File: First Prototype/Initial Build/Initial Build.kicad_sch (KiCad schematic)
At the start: 33 parts, among them J2 Conn_02x04_Odd_Even, Q1 MPSA44, Q2 BC328, Q3 BC517, U1 TLC555xP, U2 TLC555xP

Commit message: added pic
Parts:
- added C8: 47n, Capacitor_THT:C_Disc_D6.0mm_W2.5mm_P5.00mm, symbol Device:C
- added J1: Conn_01x06, symbol Connector_Generic:Conn_01x06
- added R13, R14, R15: 330k, Capacitor_SMD:C_0805_2012Metric, symbol Device:R
- added R16: 3k9, Capacitor_SMD:C_0805_2012Metric, symbol Device:R
- added R17, R18: 10k, Capacitor_SMD:C_0805_2012Metric, symbol Device:R
- added U3: PIC12F1822-ISN, Package_DIP:DIP-8_W7.62mm, symbol MCU_Microchip_PIC12:PIC12F1822-ISN
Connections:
- net +3.3VA: now also C8.1, J1.2 (Pin_2), U3.1 (VDD)
- net 400V: now also R13.1
- net GND: now also C8.2, J1.3 (Pin_3), R16.2, U3.8 (VSS)
- net Pulse A: now also U3.5 (RA2)
- net Pulse B: now also J1.1 (Pin_1), U3.4 (RA3)
- net PWM: now reaches Q1.2 (B), R2.1, U1.7 (DIS)
- net PWM: now also U3.2 (RA5)
- new net: R15.2, R16.1, U3.3 (RA4)
- new net: R13.2, R14.1
- new net: R14.2, R15.1
- new net: J1.4 (Pin_4), R17.2, U3.7 (RA0)
- new net: J1.5 (Pin_5), R18.2, U3.6 (RA1)
- new net USART_RX: R18.1
- new net USART_TX: R17.1
- no-connect marks 5 -> 6

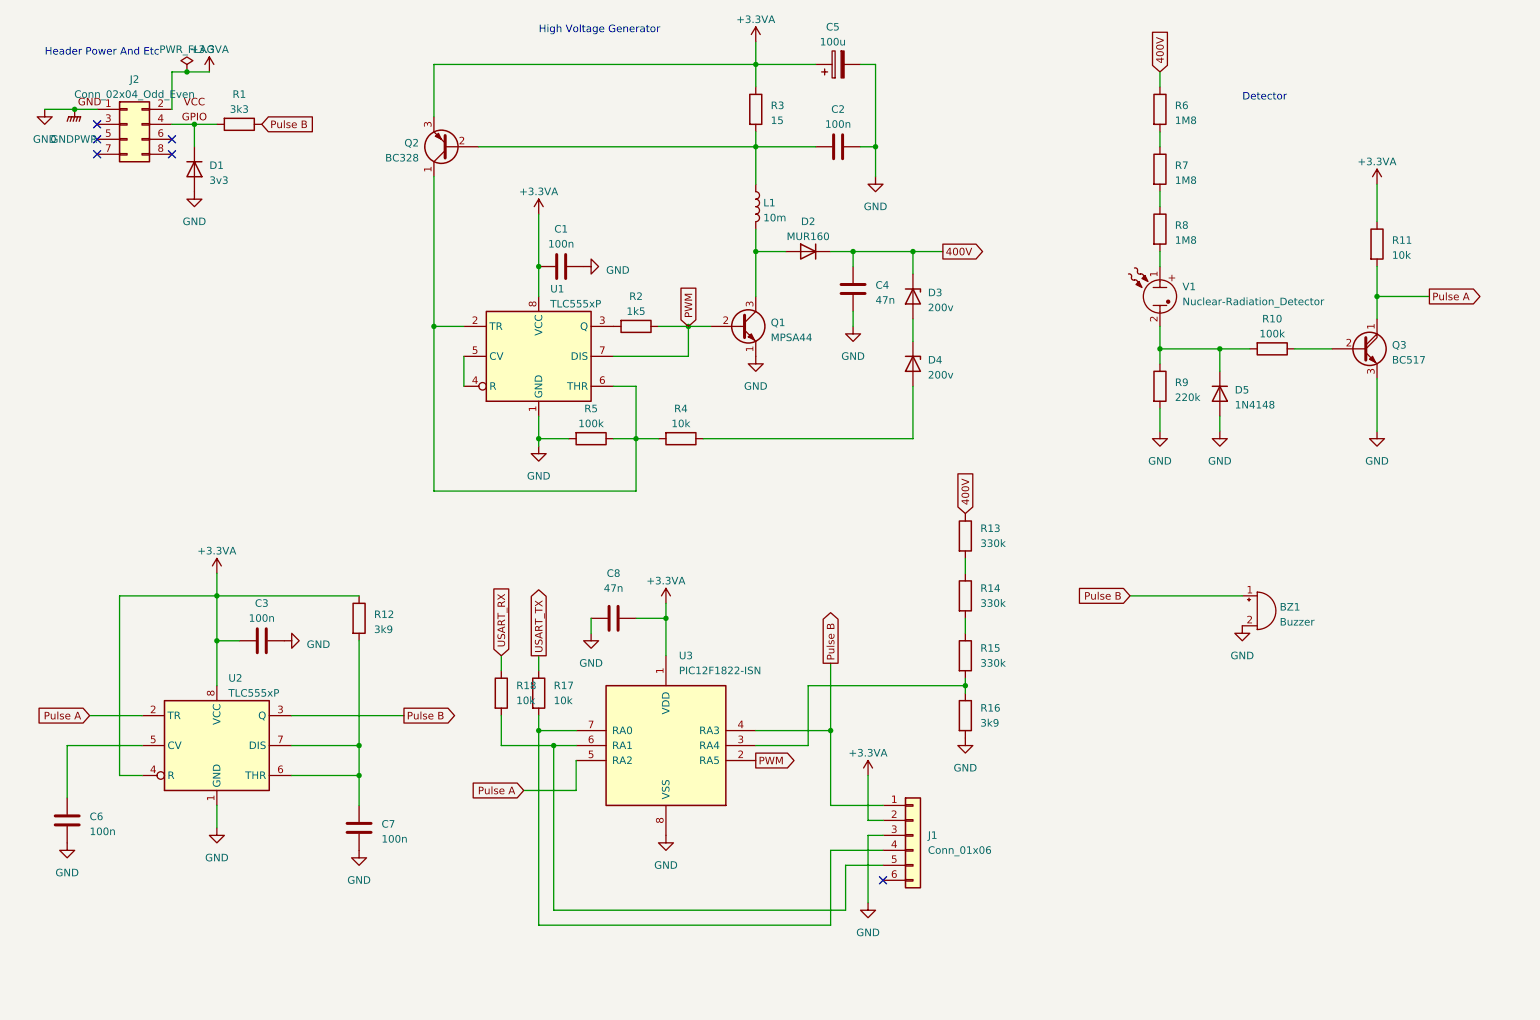
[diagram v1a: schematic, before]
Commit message: removed non-pic related components added indicator for 400v
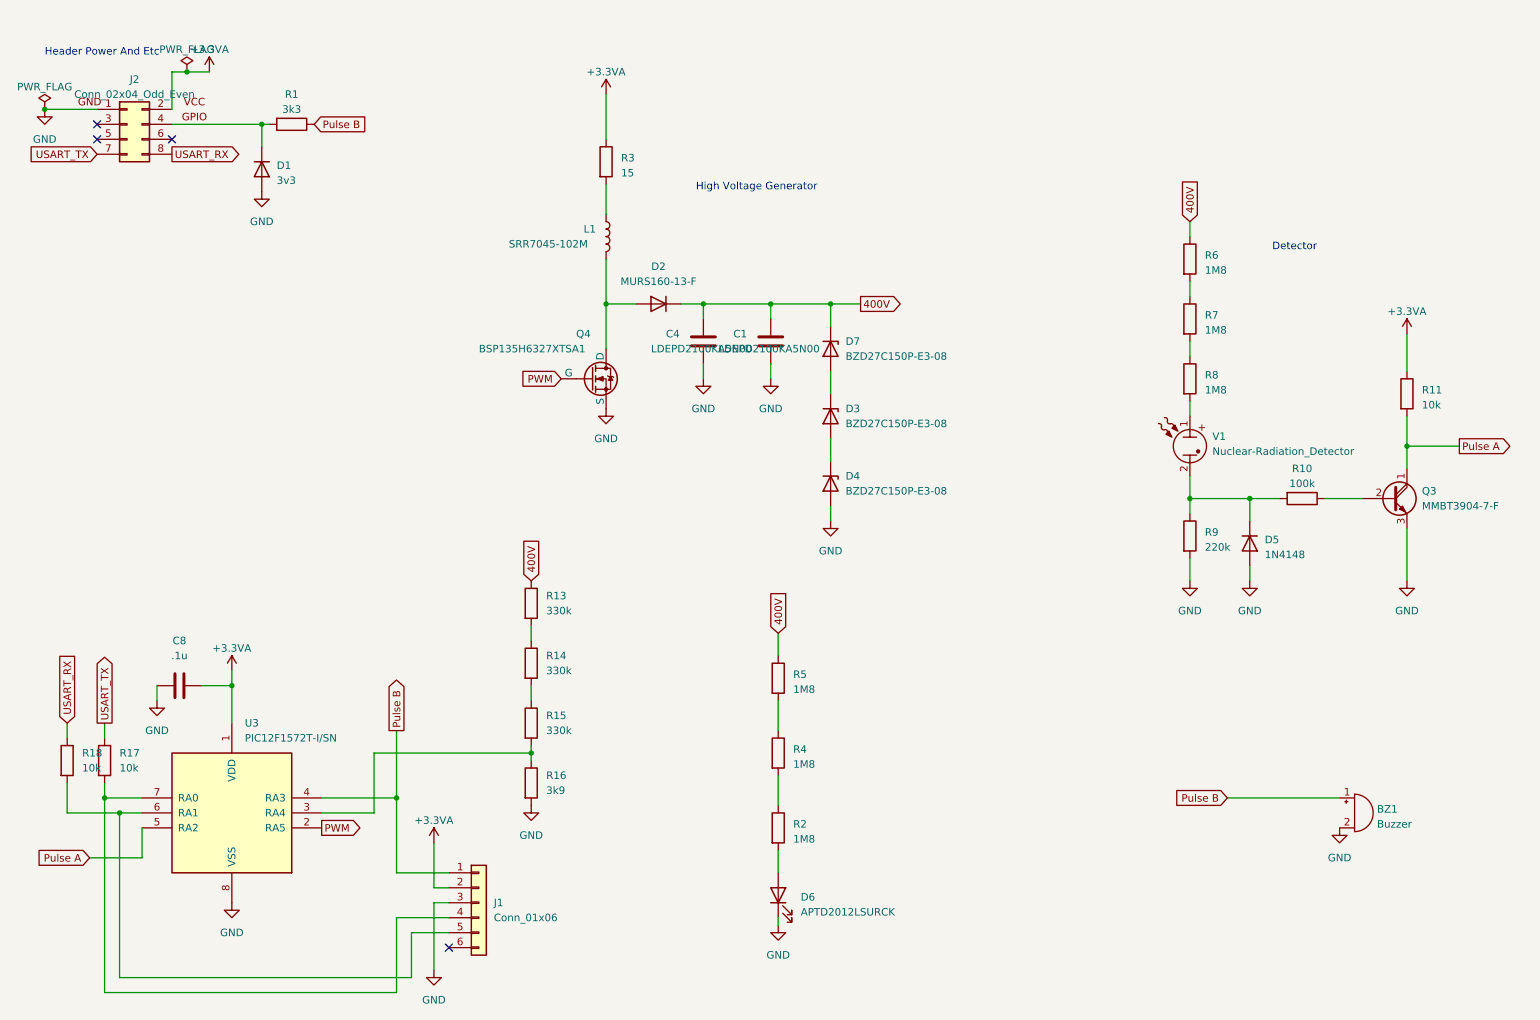
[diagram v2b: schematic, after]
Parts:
- removed C2: 100n, Capacitor_THT:C_Disc_D6.0mm_W4.4mm_P5.00mm, symbol Device:C
- removed C3, C6, C7: 100n, Capacitor_SMD:C_0805_2012Metric, symbol Device:C
- removed C5: 100u, Capacitor_THT:C_Disc_D6.0mm_W2.5mm_P5.00mm, symbol Device:C_Polarized
- removed D3, D4: 200v, Diode_SMD:D_SMF, symbol Device:D_Zener
- removed Q1: MPSA44, Package_TO_SOT_THT:TO-92_Inline, symbol Transistor_BJT:MPSA42
- removed Q2: BC328, Package_TO_SOT_THT:TO-92_Inline, symbol Transistor_BJT:BC328
- removed R12: 3k9, Capacitor_SMD:C_0805_2012Metric, symbol Device:R
- removed U1, U2: TLC555xP, Package_DIP:DIP-8_W7.62mm, symbol Timer:TLC555xP
- added D3, D4, D7: BZD27C150P-E3-08, Diode_SMD:D_SMF, symbol Diode:BZD27Cxx
- added D6: APTD2012LSURCK, LED_SMD:LED_0805_2012Metric_Pad1.15x1.40mm_HandSolder, symbol Device:LED
- added Q4: BSP135H6327XTSA1, Package_TO_SOT_SMD:SOT-223, symbol Simulation_SPICE:NMOS
- C1: value 100n -> LDEPD2100KA5N00; footprint Capacitor_SMD:C_0805_2012Metric -> Capacitor_SMD:C_2220_5650Metric_Pad1.97x5.40mm_HandSolder
- C4: value 47n -> LDEPD2100KA5N00; footprint Capacitor_THT:C_Disc_D6.0mm_W2.5mm_P5.00mm -> Capacitor_SMD:C_2220_5650Metric_Pad1.97x5.40mm_HandSolder
- C8: value 47n -> .1u; footprint Capacitor_THT:C_Disc_D6.0mm_W2.5mm_P5.00mm -> Capacitor_SMD:C_0805_2012Metric_Pad1.18x1.45mm_HandSolder
- D1: footprint Diode_SMD:D_SOD-123F -> Diode_SMD:D_SMB-SMC_Universal_Handsoldering
- D2: value MUR160 -> MURS160-13-F; footprint Diode_THT:D_DO-41_SOD81_P10.16mm_Horizontal -> Diode_SMD:D_SMB_Handsoldering
- D5: footprint Diode_THT:D_DO-35_SOD27_P7.62mm_Horizontal -> Diode_SMD:D_SMB-SMC_Universal_Handsoldering
- J1: footprint (none) -> Connector_PinHeader_2.54mm:PinHeader_1x06_P2.54mm_Vertical
- L1: value 10m -> SRR7045-102M; footprint Inductor_THT:L_Axial_L12.0mm_D5.0mm_P5.08mm_Vertical_Fastron_MISC -> Inductor_SMD:L_7.3x7.3_H3.5
- Q3: value BC517 -> MMBT3904-7-F; footprint Package_TO_SOT_THT:TO-92_Inline -> Package_TO_SOT_SMD:SOT-23-3
- R1: footprint Resistor_SMD:R_0805_2012Metric -> Resistor_SMD:R_1206_3216Metric_Pad1.30x1.75mm_HandSolder
- R10, R11, R13, R14, R15, R16, R17, R18, R3, R6, R7, R8, R9: footprint Capacitor_SMD:C_0805_2012Metric -> Resistor_SMD:R_1206_3216Metric_Pad1.30x1.75mm_HandSolder
- R2: value 1k5 -> 1M8; footprint Capacitor_SMD:C_0805_2012Metric -> Resistor_SMD:R_1206_3216Metric_Pad1.30x1.75mm_HandSolder
- R4: value 10k -> 1M8; footprint Capacitor_SMD:C_0805_2012Metric -> Resistor_SMD:R_1206_3216Metric_Pad1.30x1.75mm_HandSolder
- R5: value 100k -> 1M8; footprint Capacitor_SMD:C_0805_2012Metric -> Resistor_SMD:R_1206_3216Metric_Pad1.30x1.75mm_HandSolder
- U3: value PIC12F1822-ISN -> PIC12F1572T-I/SN; footprint Package_DIP:DIP-8_W7.62mm -> Package_SO:SOIC-8_3.9x4.9mm_P1.27mm
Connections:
- net +3.3VA: no longer C1.2
- net 400V: now also C1.2, R5.1, D7.1 (K)
- net GND: now also D4.2 (A), D6.1 (K), Q4.3 (S); no longer R5.2
- net PWM: now also Q4.2 (G); no longer R2.1
- net USART_RX: now also J2.8 (FUTURE)
- net USART_TX: now also J2.7 (Future)
- net at D2.2 (A), L1.2: now also Q4.1 (D)
- net at R4.2: now also R2.1; no longer R5.1
- net at R2.2: now also D6.2 (A)
- net at R4.1: now also R5.2
- new net: D3.2 (A), D4.1 (K)
- new net: D3.1 (K), D7.2 (A)
- no-connect marks 6 -> 4
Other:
- moved on the sheet: BZ1, C4, C8, D1, D2, D5, J1, Q3, R1, R10, R11, R13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

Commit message: updated tube fp began routing
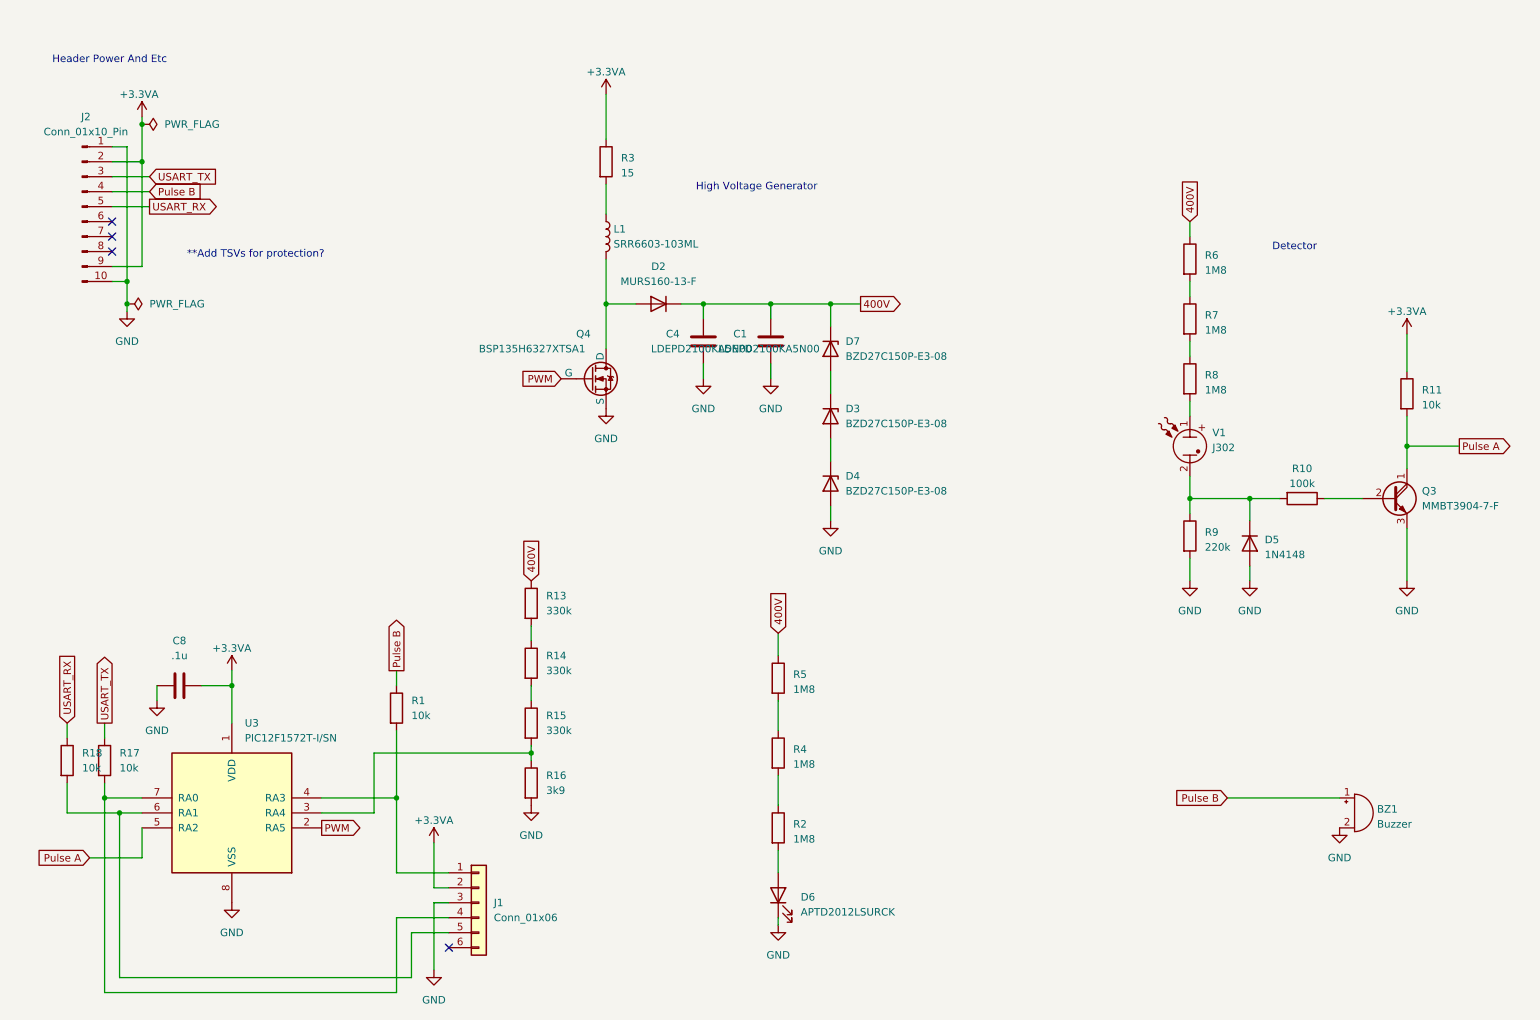
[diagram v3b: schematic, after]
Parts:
- removed D1: 3v3, Diode_SMD:D_SMB-SMC_Universal_Handsoldering, symbol Device:D
- removed J2: Conn_02x04_Odd_Even, Connector_IDC:IDC-Header_2x05_P2.54mm_Vertical, symbol Connector_Generic:Conn_02x04_Odd_Even
- added J2: Conn_01x10_Pin, Connector_PinHeader_2.54mm:PinHeader_2x05_P2.54mm_Vertical, symbol Connector:Conn_01x10_Pin
- L1: value SRR7045-102M -> SRR6603-103ML; footprint Inductor_SMD:L_7.3x7.3_H3.5 -> Inductor_SMD:L_Bourns_SRP7028A_7.3x6.6mm
- R1: value 3k3 -> 10k
- V1: value Nuclear-Radiation_Detector -> J302; footprint Geiger:Geiger Clips -> Geiger:Geiger_Clips
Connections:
- net +3.3VA: now also J2.2 (Pin_2), J2.9 (Pin_9)
- net GND: now also J2.1 (Pin_1), J2.10 (Pin_10)
- net Pulse B: now also J2.4 (Pin_4); no longer J1.1 (Pin_1), U3.4 (RA3)
- net USART_RX: now also J2.5 (Pin_5)
- net USART_TX: now also J2.3 (Pin_3)
- net at R1.2: now also J1.1 (Pin_1), U3.4 (RA3)
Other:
- note added: "**Add TSVs for protection?"

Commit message: rotated esp moved resistors away from sd card holder
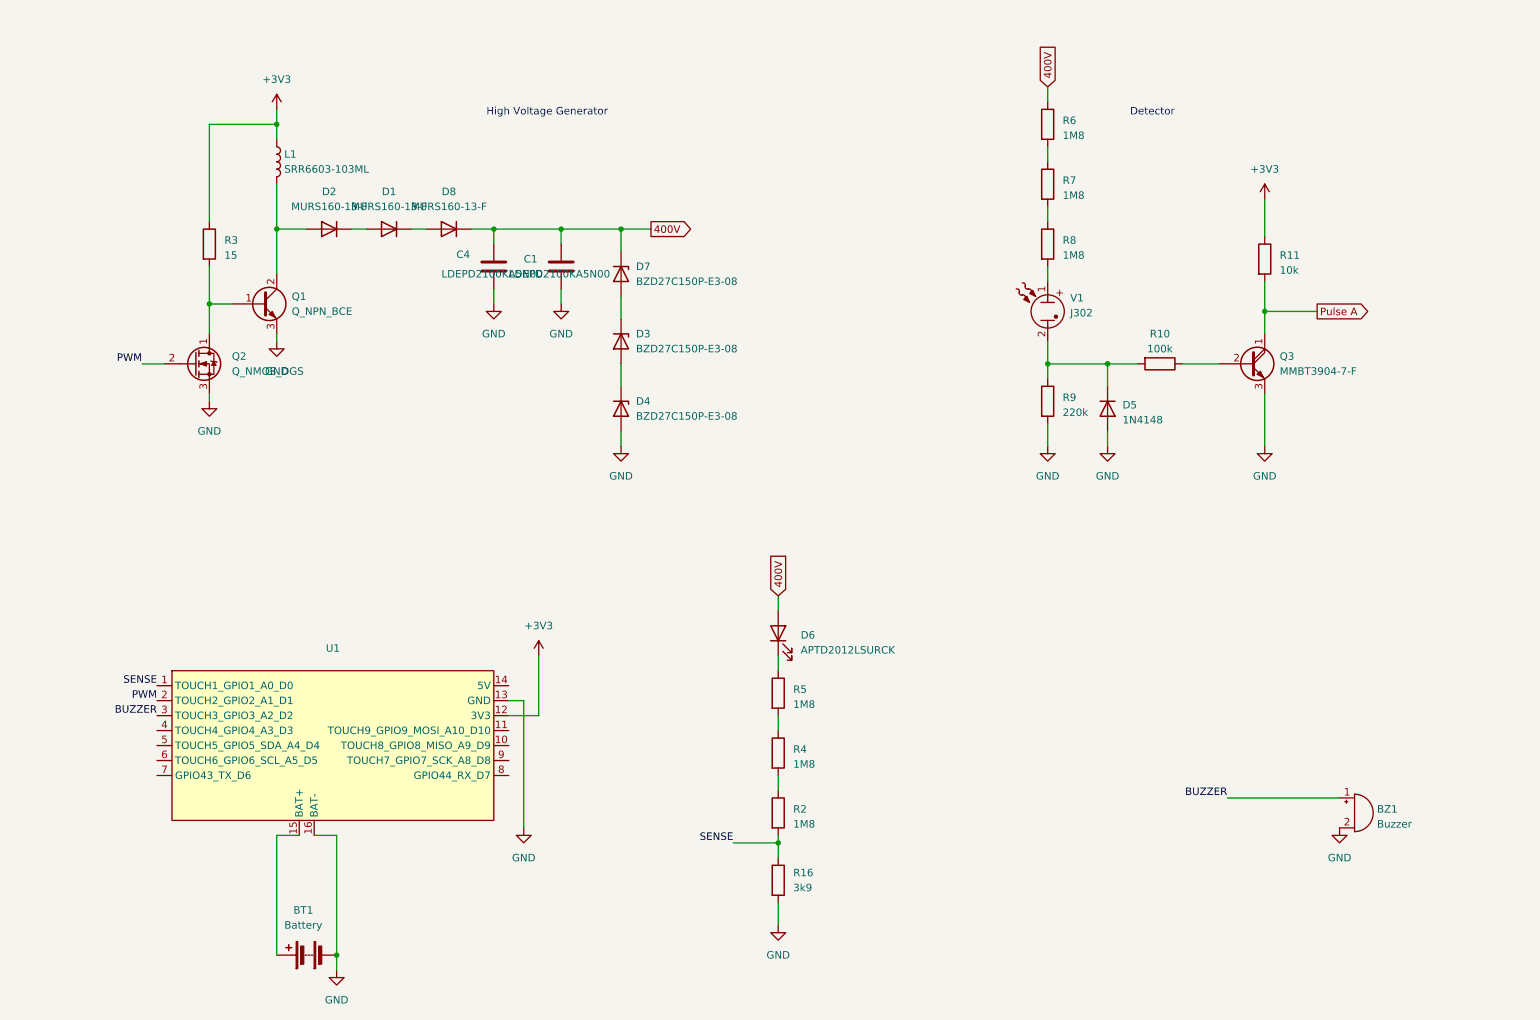
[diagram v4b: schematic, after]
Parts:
- removed C8: .1u, Capacitor_SMD:C_0805_2012Metric_Pad1.18x1.45mm_HandSolder, symbol Device:C
- removed J1: Conn_01x06, Connector_PinHeader_2.54mm:PinHeader_1x06_P2.54mm_Vertical, symbol Connector_Generic:Conn_01x06
- removed J2: Conn_01x10_Pin, Connector_PinHeader_2.54mm:PinHeader_2x05_P2.54mm_Vertical, symbol Connector:Conn_01x10_Pin
- removed Q4: BSP135H6327XTSA1, Package_TO_SOT_SMD:SOT-223, symbol Simulation_SPICE:NMOS
- removed R1, R17, R18: 10k, Resistor_SMD:R_1206_3216Metric_Pad1.30x1.75mm_HandSolder, symbol Device:R
- removed R13, R14, R15: 330k, Resistor_SMD:R_1206_3216Metric_Pad1.30x1.75mm_HandSolder, symbol Device:R
- removed U3: PIC12F1572T-I/SN, Package_SO:SOIC-8_3.9x4.9mm_P1.27mm, symbol MCU_Microchip_PIC12:PIC12F1822-ISN
- added BT1: Battery, symbol Device:Battery
- added D1, D8: MURS160-13-F, Diode_SMD:D_SMB_Handsoldering, symbol Device:D
- added Q1: Q_NPN_BCE, symbol Device:Q_NPN_BCE
- added Q2: Q_NMOS_DGS, symbol Device:Q_NMOS_DGS
- added U1: ~, symbol Seeed_Studio:ESP32S3
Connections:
- net 400V: now also D6.2 (A), D8.1 (K); no longer D2.1 (K), R5.1
- net GND: now also BT1.2 (-), Q1.3 (E), Q2.3 (S), U1.13 (GND), U1.16 (BAT-); no longer D6.1 (K)
- net PWM: now also Q2.2 (G), U1.2 (TOUCH2_GPIO2_A1_D1)
- net SENSE: now reaches R16.1
- net SENSE: now also R2.2, U1.1 (TOUCH1_GPIO1_A0_D0)
- net at R3.2: now also Q1.1 (B), Q2.1 (D); no longer L1.1
- net at D2.2 (A), L1.2: now also Q1.2 (C)
- net +3.3VA renamed +3V3
- net +3V3: now also L1.1, U1.12 (3V3)
- net Pulse B renamed BUZZER
- net BUZZER: now also U1.3 (TOUCH3_GPIO3_A2_D2)
- new net: BT1.1 (+), U1.15 (BAT+)
- new net: D6.1 (K), R5.1
- new net: D1.1 (K), D8.2 (A)
- new net: D1.2 (A), D2.1 (K)
- no-connect marks 4 -> 0
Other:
- note removed: "**Add TSVs for protection?"
- note removed: "Header Power And Etc"
- moved on the sheet: C1, C4, D2, D3, D4, D5, D6, D7, L1, Q3, R10, R11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
